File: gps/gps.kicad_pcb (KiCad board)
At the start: 2 copper layers, 167 x 82.5 mm, 69 parts, among them J1 I2C/BATT_H, J12 ENC+RGB, J13 ENC+RGB, J2 I2C/BATT_S, J3 USB_pads, J4 BATT, J5 ESP, J7 USB_B_Micro, J9 USB_pads, SW1 RotaryEncoder_Switch, SW2 MSN22AFW01, U1 NEO-M9N, U10 24C32, U11 SN74LV1T34DBVRG4, U2 TPS613222ADBVR, U3 DFR0654, U4 HT16k33, U5 7seg_1x1_rgb, U6 7seg_1x1_rgb, U7 7seg_1x1_rgb, U8 KW4-804AGB, U9 TCA39306DDFR

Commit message: added gerbers
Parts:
- added REF**: MountingHole_4.3mm_M4, MountingHole:MountingHole_4.3mm_M4, B.Cu at (195.4, 114.5)
- added REF**: MountingHole_4.3mm_M4, MountingHole:MountingHole_4.3mm_M4, B.Cu at (146.9, 70.1)
- added REF**: MountingHole_4.3mm_M4, MountingHole:MountingHole_4.3mm_M4, B.Cu at (185.5, 63.4)
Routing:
- net GND: vias 371 -> 372
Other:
- outline, holes or cut-outs redrawn
- board text added: "GNSS_Geret V.1AB"
- board text added: "GNSS_Geret V.1AT"
- board text added: "GNSS_Geret V.1BB"
- board text added: "GNSS_Geret V.1BT"
- board text added: "UP"

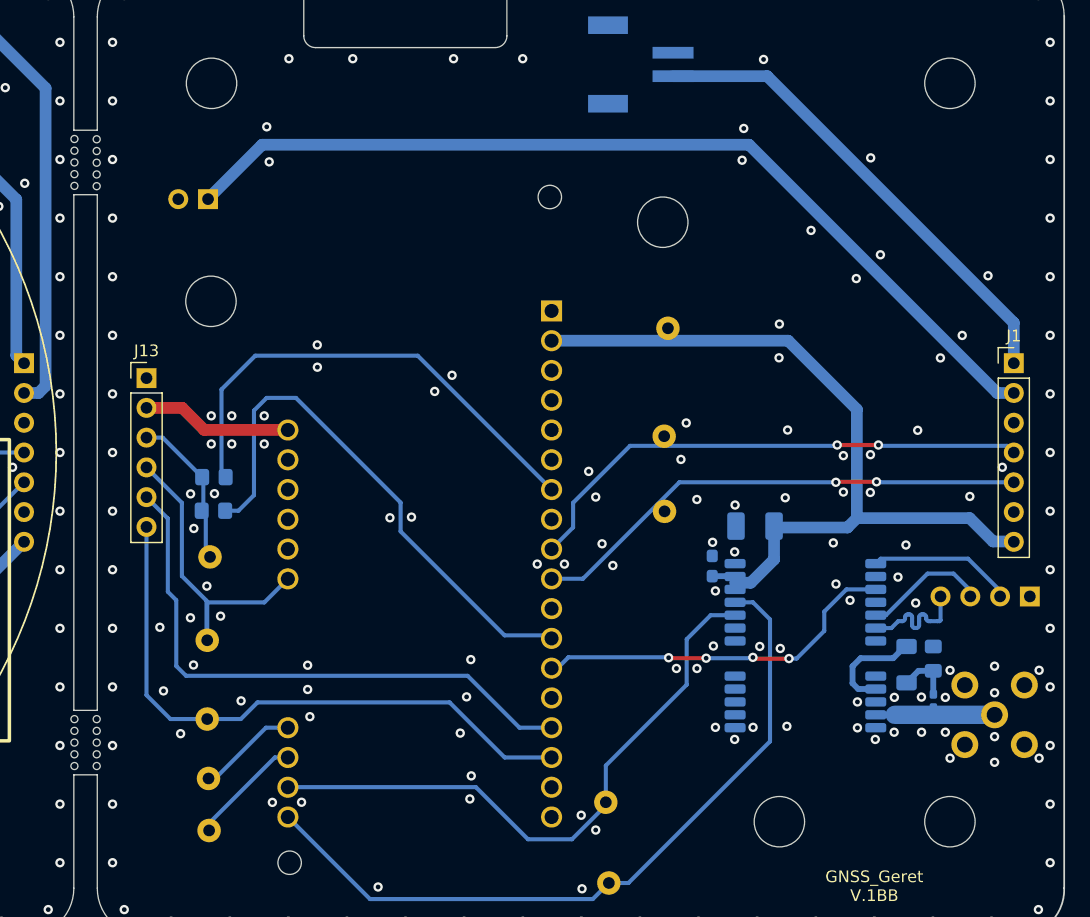
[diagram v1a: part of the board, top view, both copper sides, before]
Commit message: Final V1, cleaned display connections
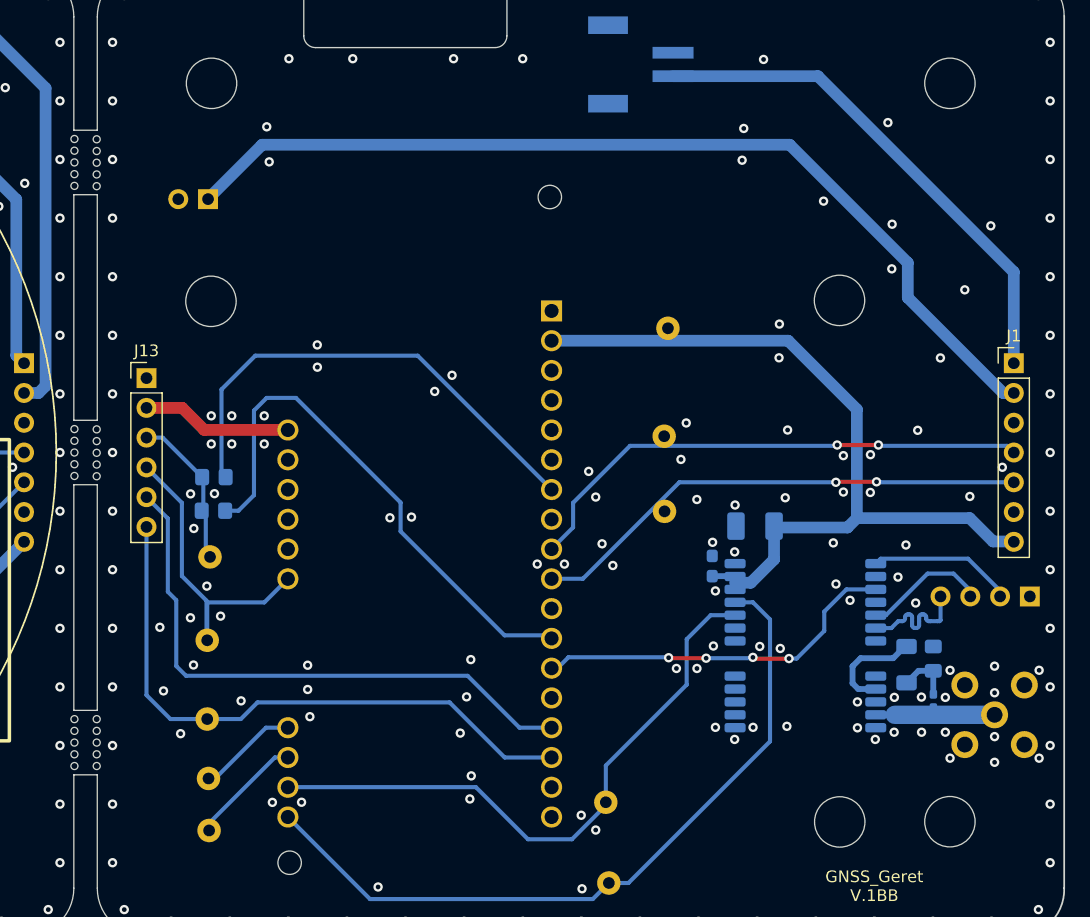
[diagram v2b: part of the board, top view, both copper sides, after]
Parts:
- moved REF** 16.5 mm to (200.6, 70.0)
- moved REF** 5.15 mm to (200.6, 114.5)
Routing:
- net SW_BATT: track 89.8 -> 92.3 mm
- net SW_ESP: track 136.9 -> 138.6 mm
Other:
- outline, holes or cut-outs redrawn
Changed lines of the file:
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@@
 	(footprint "MountingHole:MountingHole_4.3mm_M4"
 		(layer "B.Cu")
-		(at 195.45 114.5 180)
+		(at 200.6 114.52 180)
 		(descr "Mounting Hole 4.3mm, no annular, M4")
 		(tags "mounting hole 4.3mm no annular m4")
@@
 	(footprint "MountingHole:MountingHole_4.3mm_M4"
 		(layer "B.Cu")
-		(at 185.5 63.35 180)
+		(at 200.58 70.02 180)
 		(descr "Mounting Hole 4.3mm, no annular, M4")
 		(tags "mounting hole 4.3mm no annular m4")
@@
 		(layer "Edge.Cuts")
 	)
+	(gr_circle
+		(center 137.2 83.025)
+		(end 137.5 83.025)
+		(stroke
+			(width 0.1)
+			(type default)
+		)
+		(fill none)
+		(layer "Edge.Cuts")
+	)
 	(gr_arc
 		(start 155.87 48.45)
@@
 	)
 	(gr_line
+		(start 137.25 61)
+		(end 137.25 80.25)
+		(stroke
+			(width 0.1)
+			(type default)
+		)
+		(layer "Edge.Cuts")
+	)
+	(gr_circle
+		(center 137.2 81.025)
+		(end 137.5 81.025)
+		(stroke
+			(width 0.1)
+			(type default)
+		)
+		(fill none)
+		(layer "Edge.Cuts")
+	)
+	(gr_line
 		(start 135.25 110.5)
 		(end 137.25 110.5)
@@
 		(layer "Edge.Cuts")
 	)
+	(gr_line
+		(start 137.25 85.75)
+		(end 137.25 105)
+		(stroke
+			(width 0.1)
+			(type default)
+		)
+		(layer "Edge.Cuts")
+	)
+	(gr_circle
+		(center 137.2 82.025)
+		(end 137.5 82.025)
+		(stroke
+			(width 0.1)
+			(type default)
+		)
+		(fill none)
+		(layer "Edge.Cuts")
+	)
 	(gr_circle
 		(center 137.2 59.275)
@@
 		(layer "Edge.Cuts")
 	)
+	(gr_circle
+		(center 137.2 85.025)
+		(end 137.5 85.025)
+		(stroke
+			(width 0.1)
+			(type default)
+		)
+		(fill none)
+		(layer "Edge.Cuts")
+	)
 	(gr_arc
 		(start 56.578427 124.25)
@@
 	)
 	(gr_line
+		(start 135.25 105)
+		(end 135.25 85.75)
+		(stroke
+			(width 0.1)
+			(type default)
+		)
+		(layer "Edge.Cuts")
+	)
+	(gr_line
 		(start 135.25 61)
 		(end 137.25 61)
@@
 		(layer "Edge.Cuts")
 	)
+	(gr_circle
+		(center 135.3 82)
+		(end 135.6 82)
+		(stroke
+			(width 0.1)
+			(type default)
+		)
+		(fill none)
+		(layer "Edge.Cuts")
+	)
 	(gr_arc
 		(start 219.75 120.171573)
@@
 		(layer "Edge.Cuts")
 	)
-	(gr_line
-		(start 137.25 105)
-		(end 137.25 61)
-		(stroke
-			(width 0.1)
-			(type default)
-		)
-		(layer "Edge.Cuts")
-	)
 	(gr_circle
 		(center 137.2 58.275)
@@
 		(layer "Edge.Cuts")
 	)
+	(gr_circle
+		(center 135.3 85)
+		(end 135.6 85)
+		(stroke
+			(width 0.1)
+			(type default)
+		)
+		(fill none)
+		(layer "Edge.Cuts")
+	)
 	(gr_arc
 		(start 135.25 120.171573)
@@
 		(layer "Edge.Cuts")
 	)
+	(gr_circle
+		(center 135.3 84)
+		(end 135.6 84)
+		(stroke
+			(width 0.1)
+			(type default)
+		)
+		(fill none)
+		(layer "Edge.Cuts")
+	)
 	(gr_line
 		(start 154.87 42.75)
@@
 	)
 	(gr_line
+		(start 135.25 85.75)
+		(end 137.25 85.75)
+		(stroke
+			(width 0.1)
+			(type default)
+		)
+		(layer "Edge.Cuts")
+	)
+	(gr_line
 		(start 215.75 41.75)
 		(end 173.2 41.75)
@@
 	)
 	(gr_line
-		(start 135.25 61)
-		(end 135.25 105)
-		(stroke
-			(width 0.1)
-			(type default)
-		)
-		(layer "Edge.Cuts")
-	)
-	(gr_line
 		(start 135.25 55.5)
 		(end 137.25 55.5)
@@
 		(layer "Edge.Cuts")
 	)
+	(gr_circle
+		(center 135.3 83)
+		(end 135.6 83)
+		(stroke
+			(width 0.1)
+			(type default)
+		)
+		(fill none)
+		(layer "Edge.Cuts")
+	)
 	(gr_arc
 		(start 172.2 42.75)
@@
 	)
 	(gr_circle
+		(center 135.3 81)
+		(end 135.6 81)
+		(stroke
+			(width 0.1)
+			(type default)
+		)
+		(fill none)
+		(layer "Edge.Cuts")
+	)
+	(gr_circle
 		(center 135.3 107.75)
 		(end 135.6 107.75)
@@
 	)
 	(gr_circle
+		(center 137.2 84.025)
+		(end 137.5 84.025)
+		(stroke
+			(width 0.1)
+			(type default)
+		)
+		(fill none)
+		(layer "Edge.Cuts")
+	)
+	(gr_line
+		(start 135.25 80.25)
+		(end 137.25 80.25)
+		(stroke
+			(width 0.1)
+			(type default)
+		)
+		(layer "Edge.Cuts")
+	)
+	(gr_circle
 		(center 135.3 105.75)
 		(end 135.6 105.75)
@@
 		(layer "Edge.Cuts")
 	)
+	(gr_line
+		(start 135.25 61)
+		(end 135.25 80.25)
+		(stroke
+			(width 0.1)
+			(type default)
+		)
+		(layer "Edge.Cuts")
+	)
 	(gr_circle
 		(center 137.201976 109.75)
@@
 	)
 	(via
-		(at 204.07 66.13)
+		(at 205.07 63.52)
 		(size 0.8)
 		(drill 0.4)
@@
 	)
 	(via
-		(at 198.15 64.05)
+		(at 199.22 61.55)
 		(size 0.8)
 		(drill 0.4)
@@
 	)
 	(via
-		(at 213.25 67.92)
+		(at 213.49 63.66)
 		(size 0.8)
 		(drill 0.4)
@@
 	)
 	(via
-		(at 202.01 68.1575)
+		(at 205.04 67.33)
 		(size 0.8)
 		(drill 0.4)
@@
 	)
 	(via
-		(at 203.24 57.86)
+		(at 204.71 54.85)
 		(size 0.8)
 		(drill 0.4)
@@
 	)
 	(via
-		(at 211.05 73.01)
+		(at 211.27 69.12)
 		(size 0.8)
 		(drill 0.4)
@@
 	)
 	(segment
-		(start 215.45 71.93)
-		(end 194.41 50.89)
-		(width 1)
-		(layer "B.Cu")
-		(net 24)
-	)
-	(segment
 		(start 130.34 61.41)
 		(end 130.34 74.72007)
@@
 	)
 	(segment
+		(start 215.45 67.6)
+		(end 198.74 50.89)
+		(width 1)
+		(layer "B.Cu")
+		(net 24)
+	)
+	(segment
 		(start 130.34 74.72007)
 		(end 130.99993 75.38)
@@
 	)
 	(segment
-		(start 194.41 50.89)
-		(end 186.378 50.89)
+		(start 215.45 75.38)
+		(end 215.45 67.6)
 		(width 1)
 		(layer "B.Cu")
@@
 	)
 	(segment
-		(start 215.45 75.38)
-		(end 215.45 71.93)
+		(start 198.74 50.89)
+		(end 186.378 50.89)
 		(width 1)
 		(layer "B.Cu")
@@
 	)
 	(segment
-		(start 214.04 77.92)
-		(end 192.86 56.74)
+		(start 122.17 47.19)
+		(end 128.12 47.19)
 		(width 1)
 		(layer "B.Cu")
@@
 	)
 	(segment
-		(start 122.17 47.19)
-		(end 128.12 47.19)
+		(start 206.405 66.815)
+		(end 196.33 56.74)
 		(width 1)
 		(layer "B.Cu")
@@
 	)
 	(segment
-		(start 146.84 61.215)
-		(end 146.84 61.24)
+		(start 215.45 77.92)
+		(end 214.54 77.92)
 		(width 1)
 		(layer "B.Cu")
@@
 	)
 	(segment
-		(start 215.45 77.92)
-		(end 214.04 77.92)
+		(start 146.84 61.215)
+		(end 146.84 61.24)
+		(width 1)
+		(layer "B.Cu")
+		(net 56)
+	)
+	(segment
+		(start 196.33 56.74)
+		(end 151.315 56.74)
+		(width 1)
+		(layer "B.Cu")
+		(net 56)
+	)
+	(segment
+		(start 214.54 77.92)
+		(end 206.405 69.785)
 		(width 1)
 		(layer "B.Cu")
@@
 	)
 	(segment
-		(start 132.84 77.32)
-		(end 132.24 77.92)
+		(start 206.405 69.785)
+		(end 206.405 66.815)
 		(width 1)
 		(layer "B.Cu")
@@
 	)
 	(segment
-		(start 192.86 56.74)
-		(end 151.315 56.74)
+		(start 132.84 77.32)
+		(end 132.24 77.92)
 		(width 1)
 		(layer "B.Cu")

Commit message: cleaned schematic
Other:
- board text added: "BATTERY 9,5x55x65"
- board text removed: "BATT 9,5x55x65"

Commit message: updated pdf/
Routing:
- net SW_ESP: track 138.6 -> 141.6 mm
